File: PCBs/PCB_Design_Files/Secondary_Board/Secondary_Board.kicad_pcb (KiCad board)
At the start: 4 copper layers, 57.1 x 40.3 mm, 48 parts, among them IC1 TLV2333IDGKR, J1 Conn_FFC_8pin, J2 Conn_01x08_Pin, Q1 DMMT3904W-7-F, Q2 DMMT3904W-7-F, Q3 MMBT3904, Q4 MMBT3904, Q5 2N7002, Q6 BSS84, Q7 2N7002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

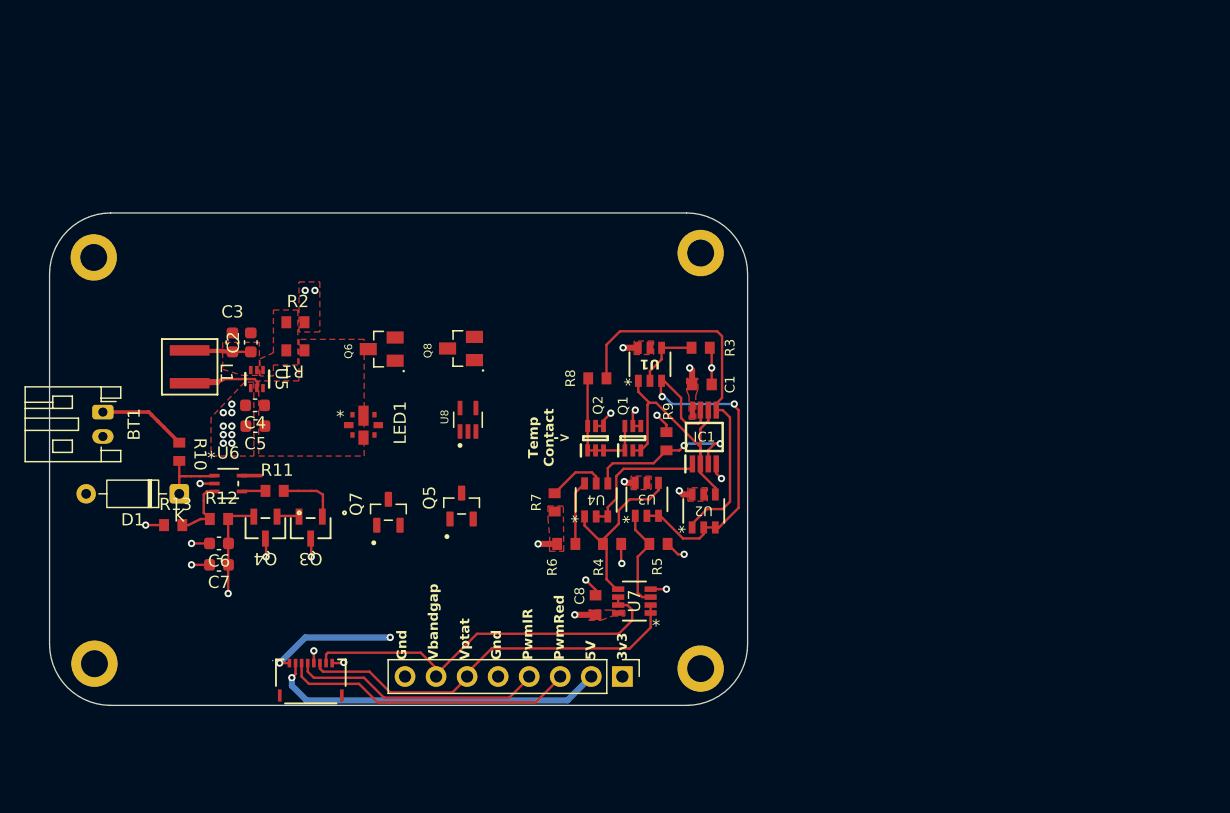
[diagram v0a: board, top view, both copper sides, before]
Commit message: updated ptat_bandgap schematic and layout. Fixed +3v3 and +5V flags
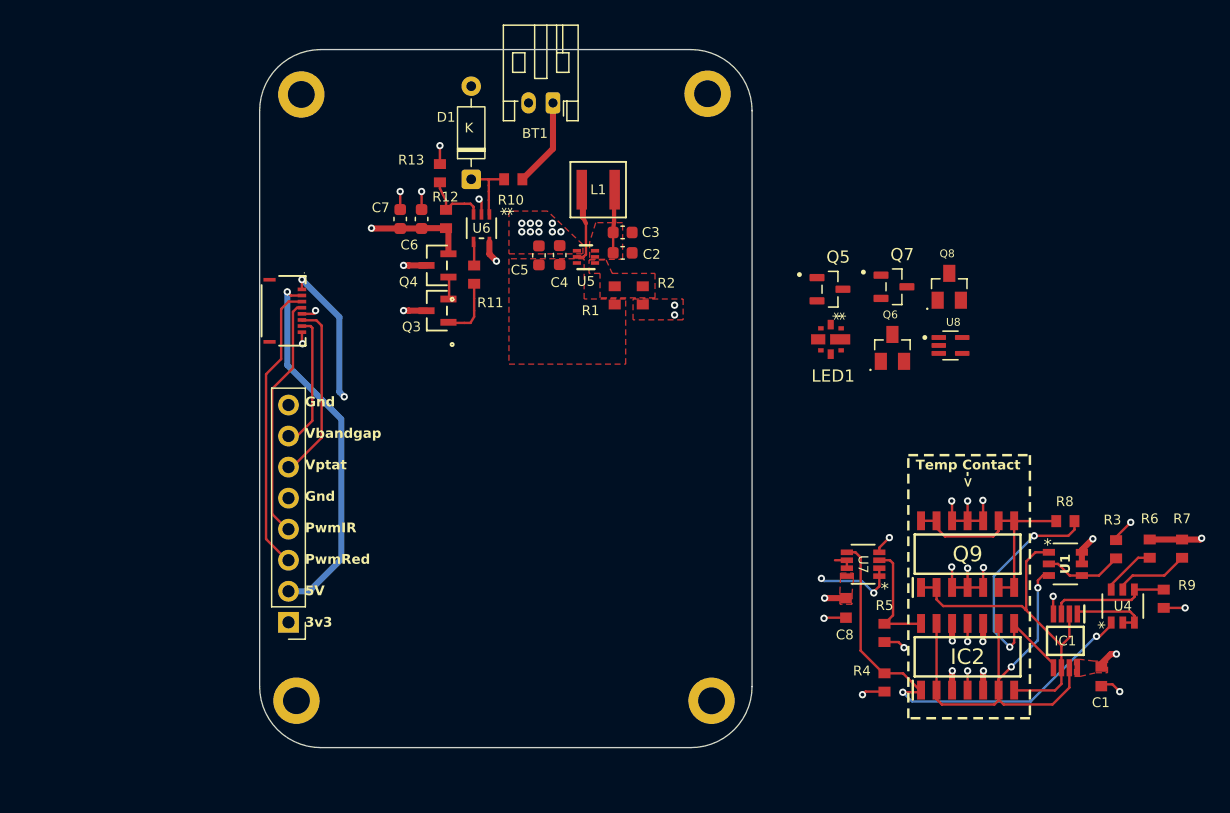
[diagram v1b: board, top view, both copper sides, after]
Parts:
- removed Q1, Q2: DMMT3904W-7-F, Project Footprints:DMMT3904W_Dual_NPN
- removed U2, U3: DMMT5401-7-F, Project Footprints:DMMT5401_Dual_PNP
- added IC2: 320S14-U, Project Footprints:That320_pnp, F.Cu at (165.5, 94.2)
- added Q9: 300S14-U, Project Footprints:That300_npn, F.Cu at (165.5, 85.8)
- moved H1 52.0 mm to (144.2, 48.1), turned to 0 degrees
- moved R7 51.5 mm to (183.1, 85.3), turned to -90 degrees
- moved H2 49.6 mm to (111.0, 48.2), turned to 0 degrees
- moved R6 47.7 mm to (180.4, 85.3), turned to -90 degrees
- moved Q7 45.3 mm to (159.5, 63.9), turned to 0 degrees
- moved BT1 44.7 mm to (131.6, 48.9), turned to 180 degrees
- moved U4 44.0 mm to (178.2, 90.0)
- moved R9 42.7 mm to (181.5, 89.4), turned to -90 degrees
- moved Q6 41.8 mm to (159.3, 68.9), turned to 0 degrees
- moved C1 40.5 mm to (176.4, 95.8), turned to 90 degrees
- moved Q8 40.3 mm to (164.0, 63.9), turned to 0 degrees
- moved R8 40.0 mm to (173.5, 83.1)
- moved U8 39.9 mm to (164.1, 68.7), turned to 0 degrees
- moved LED1 38.9 mm to (154.3, 68.2), turned to -90 degrees
- moved R3 37.8 mm to (177.7, 85.4), turned to 90 degrees
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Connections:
- net Net-(IC1-+IN_B) renamed /PTAT_Bandgap/Pnp_In+
- net Net-(IC1--IN_A) renamed /PTAT_Bandgap/Pnp_In-
- net Net-(IC1-OUT_B) renamed /PTAT_Bandgap/Pnp_base
- C4 pad 1: /Power Management/+5V -> +5V
- C5 pad 1: /Power Management/+5V -> +5V
- C6 pad 1: /Power Management/3V3 -> +3V3
- C7 pad 1: /Power Management/3V3 -> +3V3
- Q3 pad 3: /Power Management/+5V -> +5V
- Q4 pad 2: /Power Management/3V3 -> +3V3
- Q4 pad 3: /Power Management/+5V -> +5V
- R1 pad 1: /Power Management/+5V -> +5V
- R12 pad 2: /Power Management/3V3 -> +3V3
- U5 pad 6: /Power Management/+5V -> +5V
- U6 pad 5: /Power Management/+5V -> +5V
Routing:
- net /PTAT_Bandgap/Vbg: track 15.4 -> 37.0 mm, vias 0 -> 2
- net /V_bandgap: track 32.5 -> 13.3 mm
- net +3V3: track 18.8 -> 36.3 mm, vias 9 -> 11
- net GND: track 18.0 -> 34.2 mm, vias 26 -> 33
- net /V_ptat: track 33.0 -> 23.2 mm, vias 0 -> 2
- net /PTAT_Bandgap/Pnp_In+: track 31.5 -> 22.5 mm, vias 0 -> 2
- net Net-(Q9-B2): track 11.0 -> 19.7 mm
- net +5V: track 27.8 -> 36.0 mm, vias 1 -> 4
- net /PTAT_Bandgap/Pnp_In-: track 21.7 -> 29.6 mm
- net +3.7V: track 1.73 -> 9.01 mm
- net /PTAT_Bandgap/Pnp_base: track 32.4 -> 38.4 mm
- net Net-(IC1-OUT_A): track 11.4 -> 6.86 mm
- net Net-(IC1-+IN_A): track 13.6 -> 10.1 mm, vias 2 -> 0
- net Net-(U4-E2): track 4.80 -> 6.13 mm
- net /PTAT_Bandgap/Vptat: track 8.37 -> 9.49 mm
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- added copper zone on F.Cu, net +5V
- added copper zone on In2.Cu, net +5V
- removed copper zone on F.Cu, net /Power Management/+5V
- removed copper zone on In2.Cu, net /Power Management/+5V
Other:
- board size 57.1 x 40.3 mm -> 40.3 x 57.1 mm

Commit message: boost and ldo to bottom of board
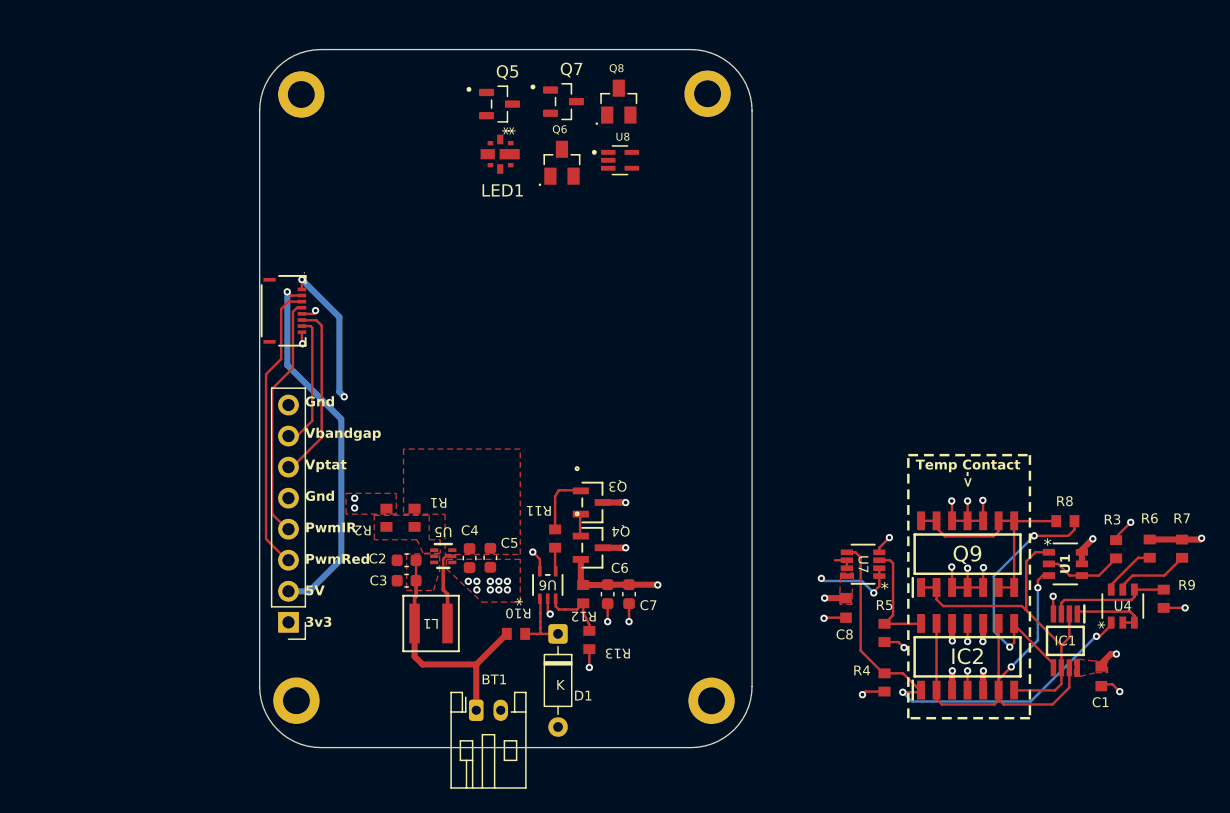
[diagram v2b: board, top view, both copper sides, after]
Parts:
- moved BT1 50.1 mm to (125.3, 98.5), turned to 0 degrees
- moved R13 40.1 mm to (134.6, 92.8), turned to 90 degrees
- moved L1 38.0 mm to (121.6, 91.5), turned to 0 degrees
- moved D1 37.9 mm to (132.0, 92.3), turned to -90 degrees
- moved R10 37.2 mm to (128.6, 92.3), turned to 0 degrees
- moved C7 36.0 mm to (137.8, 89.0), turned to -90 degrees
- moved C6 34.3 mm to (136.1, 89.0), turned to -90 degrees
- moved C3 33.5 mm to (119.6, 88.0), turned to 180 degrees
- moved R12 32.7 mm to (134.1, 89.0), turned to 90 degrees
- moved LED1 31.0 mm to (127.3, 53.0)
- moved Q5 31.0 mm to (127.2, 49.0)
- moved Q6 31.0 mm to (132.3, 53.8)
- moved U8 31.0 mm to (137.1, 53.5)
- moved Q7 31.0 mm to (132.4, 48.8)
- moved Q8 31.0 mm to (137.0, 48.8)
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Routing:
- net +3.7V: track 9.01 -> 20.6 mm
- net Net-(U5-SW): track 1.62 -> 4.51 mm

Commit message: boost to bottom
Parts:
- moved BT1 2.20 mm to (123.1, 98.5)
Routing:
- net +3.7V: track 20.6 -> 9.07 mm
- net +5V: track 36.0 -> 34.2 mm, vias 4 -> 3
- removed copper zone on In2.Cu, net +5V
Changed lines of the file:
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@@
 	(footprint "Connector_JST:JST_PH_S2B-PH-K_1x02_P2.00mm_Horizontal"
 		(layer "F.Cu")
-		(at 125.3 98.55)
+		(at 123.1 98.55)
 		(descr "JST PH series connector, S2B-PH-K (http://www.jst-mfg.com/product/pdf/eng/ePH.pdf), generated with kicad-footprint-generator")
 		(tags "connector JST PH horizontal")
@@
 	)
 	(segment
-		(start 127.8031 92.3)
-		(end 125.3 94.8031)
-		(width 0.5)
+		(start 125.65 93.85)
+		(end 125.1 94.4)
+		(width 0.3)
 		(layer "F.Cu")
 		(net 18)
 	)
 	(segment
-		(start 120.2538 94.1538)
-		(end 120.2538 91.45)
-		(width 0.5)
+		(start 127.2 92.3)
+		(end 125.65 93.85)
+		(width 0.3)
 		(layer "F.Cu")
 		(net 18)
@@
 	)
 	(segment
-		(start 120.9031 94.8031)
-		(end 120.2538 94.1538)
-		(width 0.5)
-		(layer "F.Cu")
-		(net 18)
-	)
-	(segment
 		(start 120.2538 91.45)
 		(end 120.2538 89.3462)
@@
 	)
 	(segment
-		(start 125.3 94.8031)
-		(end 125.3 98.55)
-		(width 0.5)
+		(start 125.1 94.4)
+		(end 125.1 94.6)
+		(width 0.3)
 		(layer "F.Cu")
 		(net 18)
 	)
 	(segment
-		(start 120.4 89.2)
-		(end 120.375 89.175)
+		(start 127.8031 92.3)
+		(end 127.2 92.3)
 		(width 0.3)
 		(layer "F.Cu")
@@
 	)
 	(segment
-		(start 125.3 94.8031)
-		(end 120.9031 94.8031)
-		(width 0.5)
+		(start 120.4 89.2)
+		(end 120.375 89.175)
+		(width 0.3)
 		(layer "F.Cu")
 		(net 18)
@@
 	)
 	(segment
+		(start 131.75 83.7531)
+		(end 131.75 83.675)
+		(width 0.2)
+		(layer "F.Cu")
+		(net 21)
+	)
+	(segment
 		(start 161.618 91.375)
 		(end 161.69 91.447)
@@
 	)
 	(segment
-		(start 129.93 85.6)
-		(end 129.925 85.605)
-		(width 0.5)
-		(layer "F.Cu")
-		(net 27)
-	)
-	(segment
 		(start 111.035 64.615017)
 		(end 110.135005 64.615017)
@@
 	)
 	(segment
-		(start 130.500001 87.17605)
-		(end 130.500001 86.180001)
-		(width 0.2)
-		(layer "F.Cu")
-		(net 27)
-	)
-	(segment
 		(start 137.1 81.55)
 		(end 135.64725 81.55)
@@
 		(net 27)
 	)
-	(segment
-		(start 130.500001 86.180001)
-		(end 129.925 85.605)
-		(width 0.2)
-		(layer "F.Cu")
-		(net 27)
-	)
 	(via
 		(at 109.835 64.315012)
@@
 	)
 	(via
-		(at 129.925 85.605)
-		(size 0.6)
-		(drill 0.3)
-		(layers "F.Cu" "B.Cu")
-		(net 27)
-	)
-	(via
 		(at 137.525 85.255)
 		(size 0.6)
@@
 	)
 	(zone
+		(net 18)
+		(net_name "+3.7V")
+		(layer "F.Cu")
+		(hatch edge 0.5)
+		(priority 1)
+		(connect_pads
+			(clearance 0.1)
+		)
+		(min_thickness 0.25)
+		(filled_areas_thickness no)
+		(fill yes
+			(thermal_gap 0.5)
+			(thermal_bridge_width 0.5)
+			(island_removal_mode 1)
+			(island_area_min 10)
+		)
+		(polygon
+			(pts
+				(xy 124.2 99.5) (xy 121.4 99.5) (xy 121.4 96.1) (xy 119.8 94.4) (xy 119.822 92.4) (xy 121.2 92.4)
+				(xy 121.2 94.1) (xy 122.1 94.1) (xy 126.2 94.1) (xy 127.1 94.1) (xy 126.357695 94.1) (xy 126.459402 97.240598)
+			)
+		)
+	)
+	(zone
 		(net 23)
 		(net_name "/Power Management/Vfb")
@@
 		(hatch edge 0.5)
 		(priority 9)
-		(connect_pads yes
+		(connect_pads
 			(clearance 0.1)
 		)
@@
 		(filled_areas_thickness no)
 		(fill yes
-			(thermal_gap 0.5)
-			(thermal_bridge_width 0.5)
+			(thermal_gap 0.25)
+			(thermal_bridge_width 0.3)
 			(island_removal_mode 1)
 			(island_area_min 10)
@@
 	)
 	(zone
-		(net 20)
-		(net_name "Net-(U5-SW)")
+		(net 2)
+		(net_name "GND")
 		(layer "F.Cu")
-		(name "$teardrop_padvia$")
-		(hatch none 0.1)
-		(priority 30000)
-		(attr
-			(teardrop
-				(type padvia)
-			)
-		)
-		(connect_pads yes
-			(clearance 0)
+		(hatch edge 0.5)
+		(priority 10)
+		(connect_pads
+			(clearance 0.1)
 		)
-		(min_thickness 0.0254)
+		(min_thickness 0.25)
 		(filled_areas_thickness no)
 		(fill yes
-			(thermal_gap 0.5)
-			(thermal_bridge_width 0.5)
+			(thermal_gap 0.25)
+			(thermal_bridge_width 0.3)
 			(island_removal_mode 1)
 			(island_area_min 10)
@@
 		(polygon
 			(pts
-				(xy 123.0962 89.3926) (xy 122.7962 89.3926) (xy 122.5144 89.8244) (xy 122.9462 91.451) (xy 123.378 89.8244)
+				(xy 118.75 80.8) (xy 118.75 82.5) (xy 114.65 82.5079) (xy 114.65 80.8)
 			)
 		)
 	)
 	(zone
-		(net 2)
-		(net_name "GND")
+		(net 20)
+		(net_name "Net-(U5-SW)")
 		(layer "F.Cu")
-		(hatch edge 0.5)
-		(priority 10)
+		(name "$teardrop_padvia$")
+		(hatch none 0.1)
+		(priority 30001)
+		(attr
+			(teardrop
+				(type padvia)
+			)
+		)
 		(connect_pads yes
-			(clearance 0.1)
+			(clearance 0)
 		)
-		(min_thickness 0.25)
+		(min_thickness 0.0254)
 		(filled_areas_thickness no)
 		(fill yes
@@
 		(polygon
 			(pts
-				(xy 118.75 80.8) (xy 118.75 82.5) (xy 114.65 82.5079) (xy 114.65 80.8)
+				(xy 123.0962 89.3926) (xy 122.7962 89.3926) (xy 122.5144 89.8244) (xy 122.9462 91.451) (xy 123.378 89.8244)
 			)
 		)
@@
 		(polygon
 			(pts
-				(xy 120.0038 93.5074) (xy 120.5038 93.5074) (xy 120.6856 93.0756) (xy 120.2538 91.449) (xy 119.822 93.0756)
+				(xy 120.4038 89.3926) (xy 120.1038 89.3926) (xy 119.822 89.8244) (xy 120.2538 91.451) (xy 120.6856 89.8244)
 			)
 		)
@@
 	)
 	(zone
-		(net 18)
-		(net_name "+3.7V")
-		(layer "F.Cu")
-		(name "$teardrop_padvia$")
-		(hatch none 0.1)
-		(priority 30001)
-		(attr
-			(teardrop
-				(type padvia)
-			)
-		)
-		(connect_pads yes
-			(clearance 0)
-		)
-		(min_thickness 0.0254)
-		(filled_areas_thickness no)
-		(fill yes
-			(thermal_gap 0.5)
-			(thermal_bridge_width 0.5)
-			(island_removal_mode 1)
-			(island_area_min 10)
-		)
-		(polygon
-			(pts
-				(xy 120.4038 89.3926) (xy 120.1038 89.3926) (xy 119.822 89.8244) (xy 120.2538 91.451) (xy 120.6856 89.8244)
-			)
-		)
-	)
-	(zone
 		(net 27)
 		(net_name "+5V")
@@
 		(polygon
 			(pts
-				(xy 119.35 77.175) (xy 119.35 82.5) (xy 122.75 82.5079) (xy 122.75 85.8) (xy 128.9 85.8) (xy 128.9 77.175)
+				(xy 119.3 80.7) (xy 119.35 82.5) (xy 122.75 82.5079) (xy 122.75 85.8) (xy 128.225 85.8) (xy 129.65 87.7)
+				(xy 130.7 87.7) (xy 130.7 83.876281) (xy 129.000313 80.801045)
 			)
 		)
@@
 	)
 	(zone
-		(net 27)
-		(net_name "+5V")
+		(net 1)
+		(net_name "+3V3")
 		(layer "In2.Cu")
 		(hatch edge 0.5)

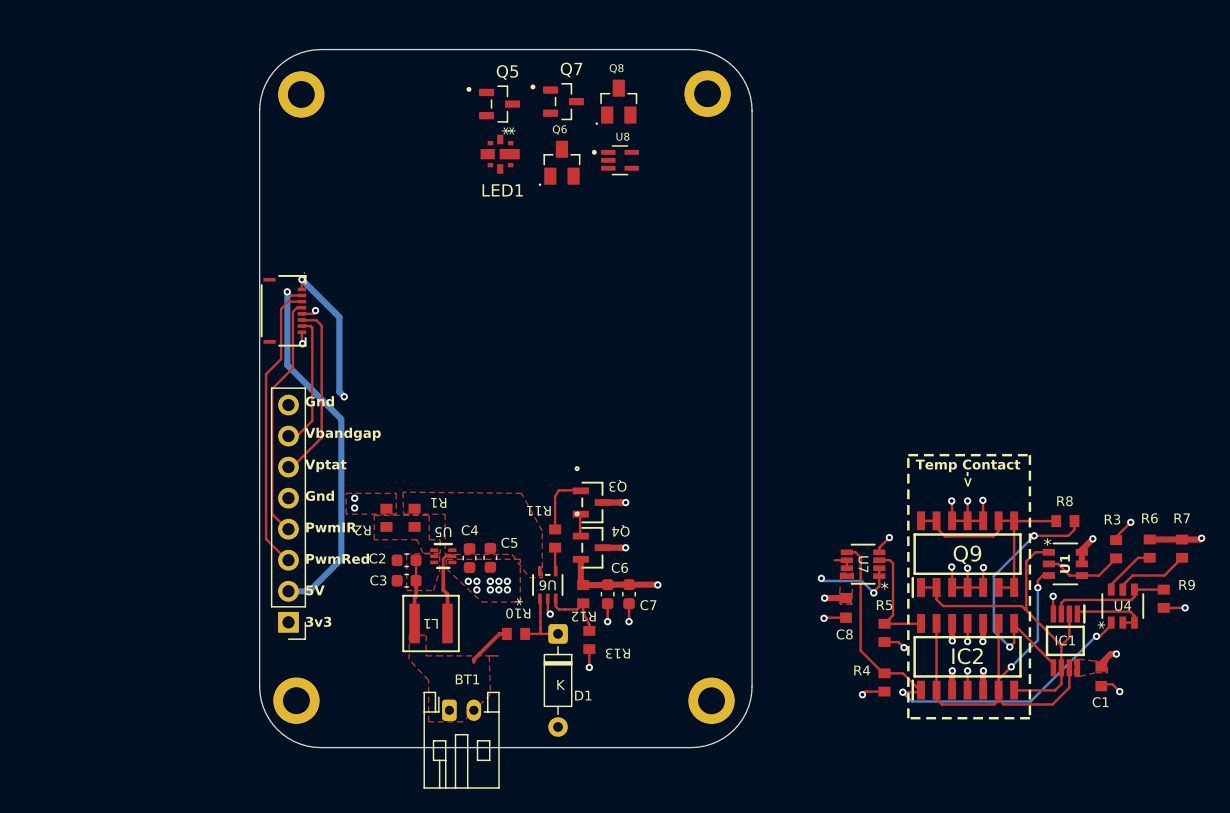
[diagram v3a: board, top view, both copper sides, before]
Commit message: secondary board rearrange
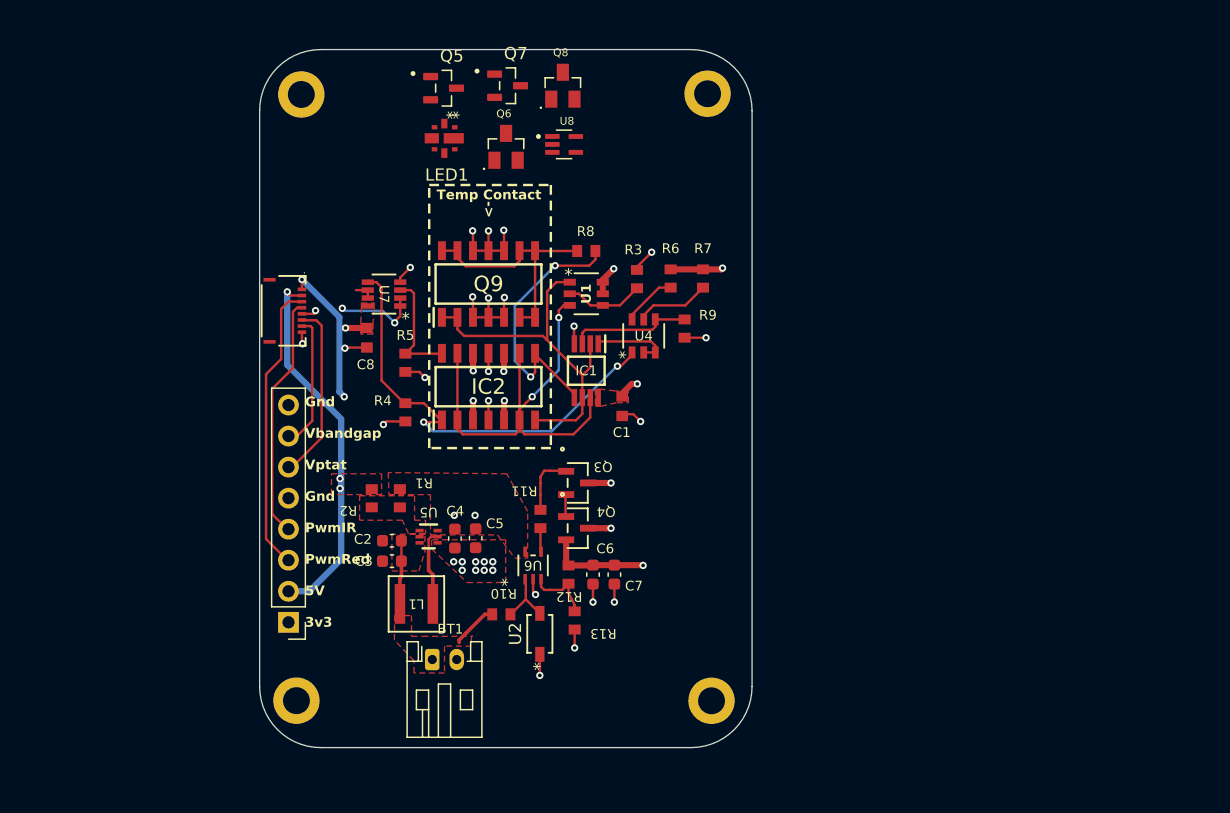
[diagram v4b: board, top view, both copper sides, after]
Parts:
- removed D1: 15N122B, Diode_THT:D_DO-35_SOD27_P7.62mm_Horizontal
- added U2: MMSZ5221BT1G, Project Footprints:SOD-123_ONS, F.Cu at (130.5, 92.3)
- moved R3 45.0 mm to (138.4, 63.3)
- moved R6 45.0 mm to (141.2, 63.2)
- moved R7 45.0 mm to (143.8, 63.2)
- moved C8 45.0 mm to (116.3, 68.1)
- moved IC2 45.0 mm to (126.3, 72.1)
- moved Q9 45.0 mm to (126.3, 63.7)
- moved C1 45.0 mm to (137.2, 73.7)
- moved IC1 45.0 mm to (134.3, 70.8)
- moved R4 45.0 mm to (119.5, 74.2)
- moved R5 45.0 mm to (119.5, 70.1)
- moved R8 45.0 mm to (134.3, 61.0)
- moved R9 45.0 mm to (142.3, 67.3)
- moved U1 45.0 mm to (134.3, 64.5)
- moved U4 45.0 mm to (139.0, 67.9)
- moved U7 45.0 mm to (117.8, 64.5)
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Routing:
- net Net-(U2-ANODE): track 0.00 -> 3.86 mm
- net GND: track 34.2 -> 36.0 mm, vias 33 -> 34
- net +5V: vias 3 -> 5
